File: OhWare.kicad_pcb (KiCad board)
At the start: 2 copper layers, 110 parts, among them J1 Screw_Terminal_01x03, J11 Screw_Terminal_01x05, J12 Conn_01x03_Pin, J13 Micro_SD_Card, J14 Screw_Terminal_01x03, J15 RJ45_Hanrun_HR911105A_Horizon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, J16 Conn_02x05_Odd_Even, J17 Conn_02x03_Odd_Even, J18 Conn_02x03_Odd_Even, J19 Conn_02x03_Odd_Even, J2 Conn_01x04_Pin, J3 Conn_01x02_Pin, J4 Conn_01x02_Pin, J5 Conn_01x04_Pin, J6 Conn_01x02_Pin, J7 8P8C_Shielded, J8 8P8C_Shielded, J9 Conn_02x05_Odd_Even, SW2 SW_DIP_x01, SW3 SW_DIP_x03, U1 STM32F407VETx, U2 SIT65HVD230DR, U3 SIT3490EESA, U4 XL1509-5.0E1, U5 AMS1117-3.3, U6 TL431M-0.3%-6AF, U7 LAN8720AI-CP-TR, U8 USB-TYPE-C-016, X1 X32258MOB4SI, X2 ABS07-32.768KHZ-T, X3 XL2EL89CSI-111YLC-25M

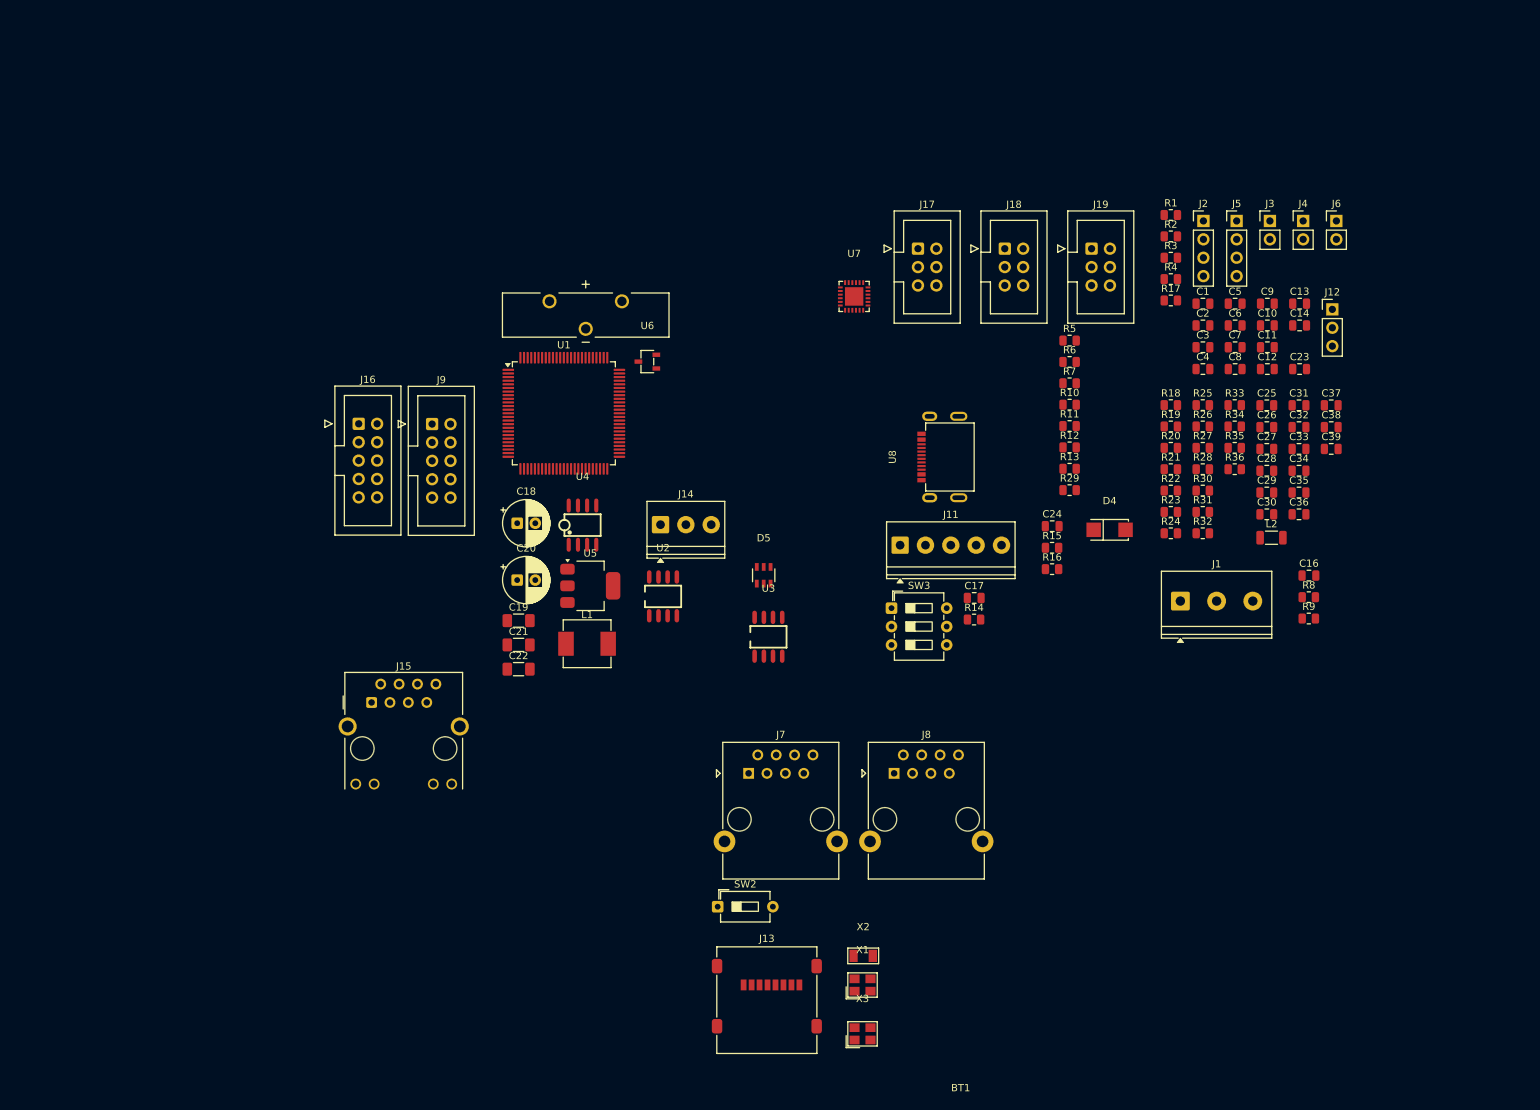
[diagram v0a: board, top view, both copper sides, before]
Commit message: Key CHanges for connector choices , termination and semi-final decisions on them
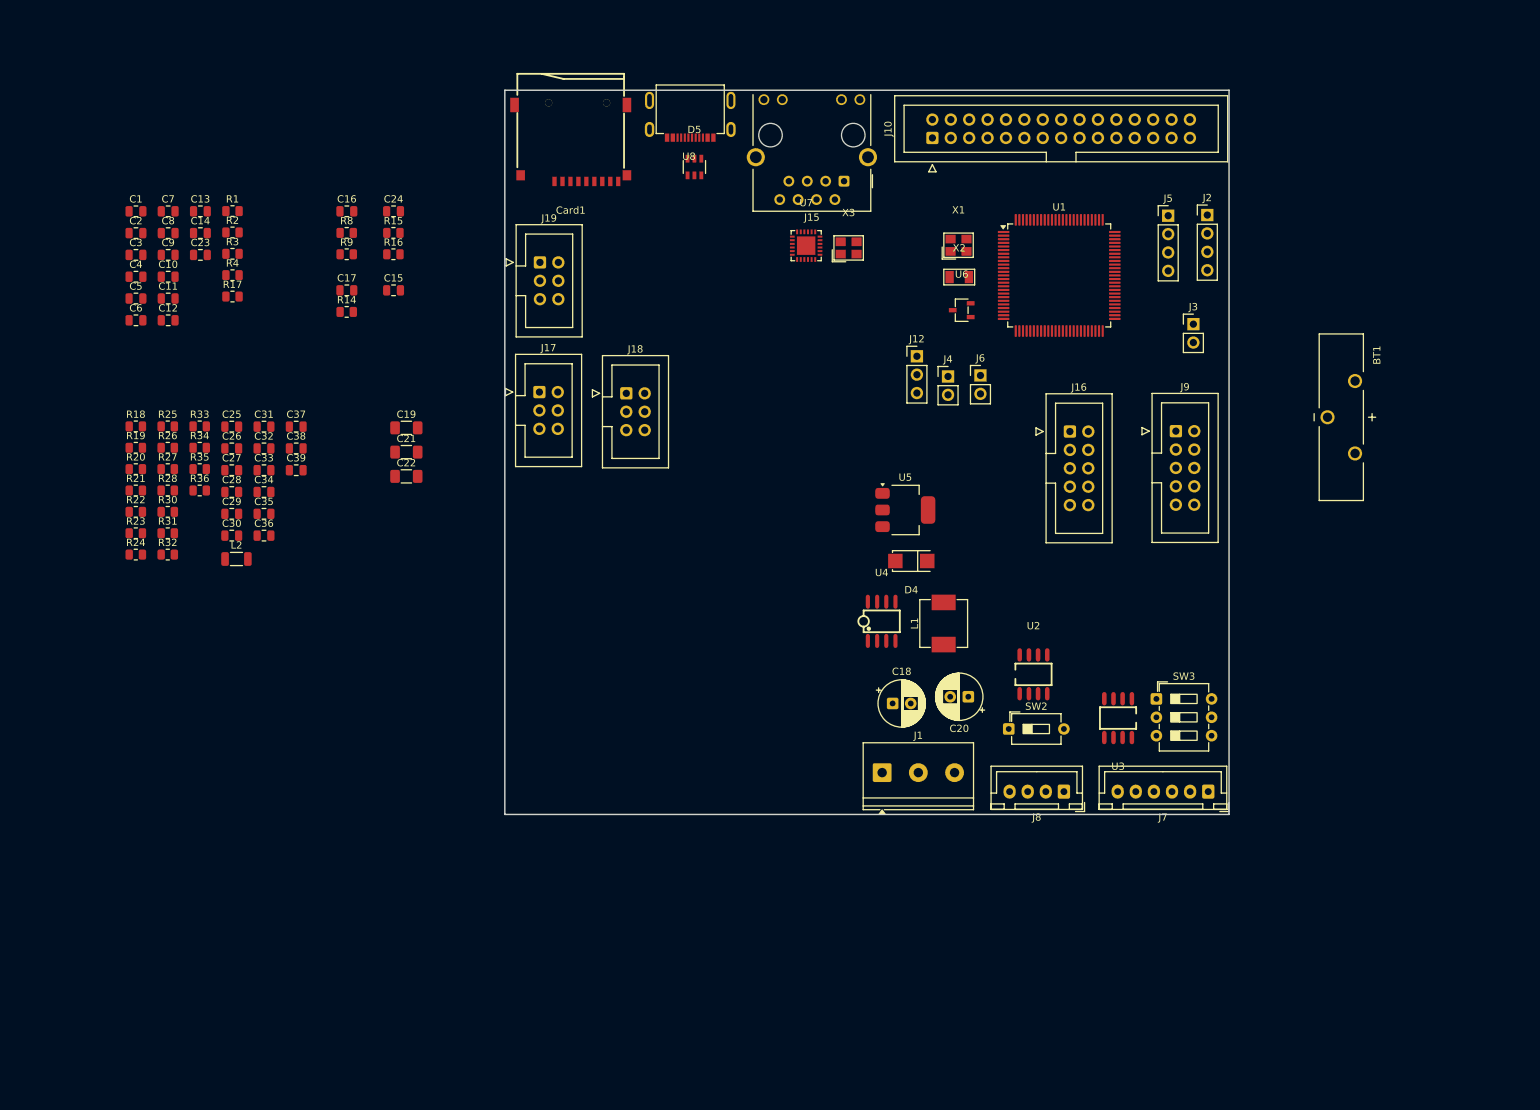
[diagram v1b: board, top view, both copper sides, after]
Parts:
- removed J11: Screw_Terminal_01x05, TerminalBlock_Phoenix:TerminalBlock_Phoenix_PT-1,5-5-3.5-H_1x05_P3.50mm_Horizontal
- removed J13: Micro_SD_Card, Connector_Card:microSD_HC_Molex_47219-2001
- removed J14: Screw_Terminal_01x03, TerminalBlock_Phoenix:TerminalBlock_Phoenix_PT-1,5-3-3.5-H_1x03_P3.50mm_Horizontal
- removed R10, R11, R12, R13, R29, R5, R6, R7: 0, Resistor_SMD:R_0805_2012Metric
- added C15: 100n, Capacitor_SMD:C_0805_2012Metric, F.Cu at (84.6, 77.6)
- added Card1: TF-01A, EasyEDA:TF-SMD_TF-01A, F.Cu at (109.1, 57.3)
- added J10: Conn_02x15_Odd_Even, Connector_IDC:IDC-Header_2x15_P2.54mm_Vertical, F.Cu at (159.0, 56.6)
- J7: value 8P8C_Shielded -> Conn_01x06_Pin; footprint Connector_RJ:RJ45_Ninigi_GE -> Connector_JST:JST_XH_B6B-XH-A_1x06_P2.50mm_Vertical
- J8: value 8P8C_Shielded -> Conn_01x04_Pin; footprint Connector_RJ:RJ45_Ninigi_GE -> Connector_JST:JST_XH_B4B-XH-A_1x04_P2.50mm_Vertical
- moved C23 152.6 mm to (58.0, 72.7)
- moved C13 152.3 mm to (58.0, 66.7)
- moved C14 152.3 mm to (58.0, 69.7)
- moved C10 151.9 mm to (53.5, 75.8)
- moved C11 151.9 mm to (53.5, 78.8)
- moved C12 151.9 mm to (53.5, 81.8)
- moved C9 151.9 mm to (53.5, 72.7)
- moved C5 151.8 mm to (49.1, 78.8)
- moved C6 151.8 mm to (49.1, 81.8)
- moved C7 148.5 mm to (53.5, 66.7)
- moved C8 148.5 mm to (53.5, 69.7)
- moved C1 147.9 mm to (49.1, 66.7)
- moved C2 147.9 mm to (49.1, 69.7)
- moved C3 147.9 mm to (49.1, 72.7)
- moved C4 147.9 mm to (49.1, 75.8)
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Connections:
- J15 pad SH: Earth -> GND
- J16 pad 3: Net-(J16-Pin_3) -> /Controller/SPI1_MOSI
- J16 pad 5: Net-(J16-Pin_5) -> /Controller/SPI1_MISO
- J16 pad 7: Net-(J16-Pin_7) -> /Controller/SPI1_SCK
- J16 pad 9: Net-(J16-Pin_9) -> /Controller/SPI1_CS2
- J7 pad 1: /CAN/CAN_H -> /RS485/Y
- J7 pad 2: /CAN/CAN_L -> /RS485/Z
- J7 pad 3: GND -> /RS485/A
- J7 pad 4: unconnected-(J7-Pad4) -> /RS485/B
- J7 pad 5: unconnected-(J7-Pad5) -> GND
- J7 pad 6: unconnected-(J7-Pad6) -> Earth
- J8 pad 4: unconnected-(J8-Pad4) -> Earth
- J9 pad 3: Net-(J9-Pin_3) -> /Controller/SPI1_MOSI
- J9 pad 5: Net-(J9-Pin_5) -> /Controller/SPI1_MISO
- J9 pad 7: Net-(J9-Pin_7) -> /Controller/SPI1_SCK
- J9 pad 9: Net-(J9-Pin_9) -> /Controller/SPI1_CS1
- U8 pad 17: Earth -> GND
- U8 pad 18: Earth -> GND
- U8 pad A1: unconnected-(U8-PadA1) -> GND
- U8 pad A12: unconnected-(U8-PadA12) -> Net-(U8-PadA12)
- U8 pad B1: unconnected-(U8-PadB1) -> Net-(U8-PadA12)
- U8 pad B12: unconnected-(U8-PadB12) -> GND
- U8 pad B6: unconnected-(U8-PadB6) -> Net-(D5-Pad3)
- U8 pad B7: unconnected-(U8-PadB7) -> Net-(D5-Pad1)
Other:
- board outline added: 100 x 100 mm

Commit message: Done routing for Buck Converter , Rs485 and CAN , Some Routing for MCU and associated circuitry , NO ETHERNET ROUTING , NO module Interconnects yet
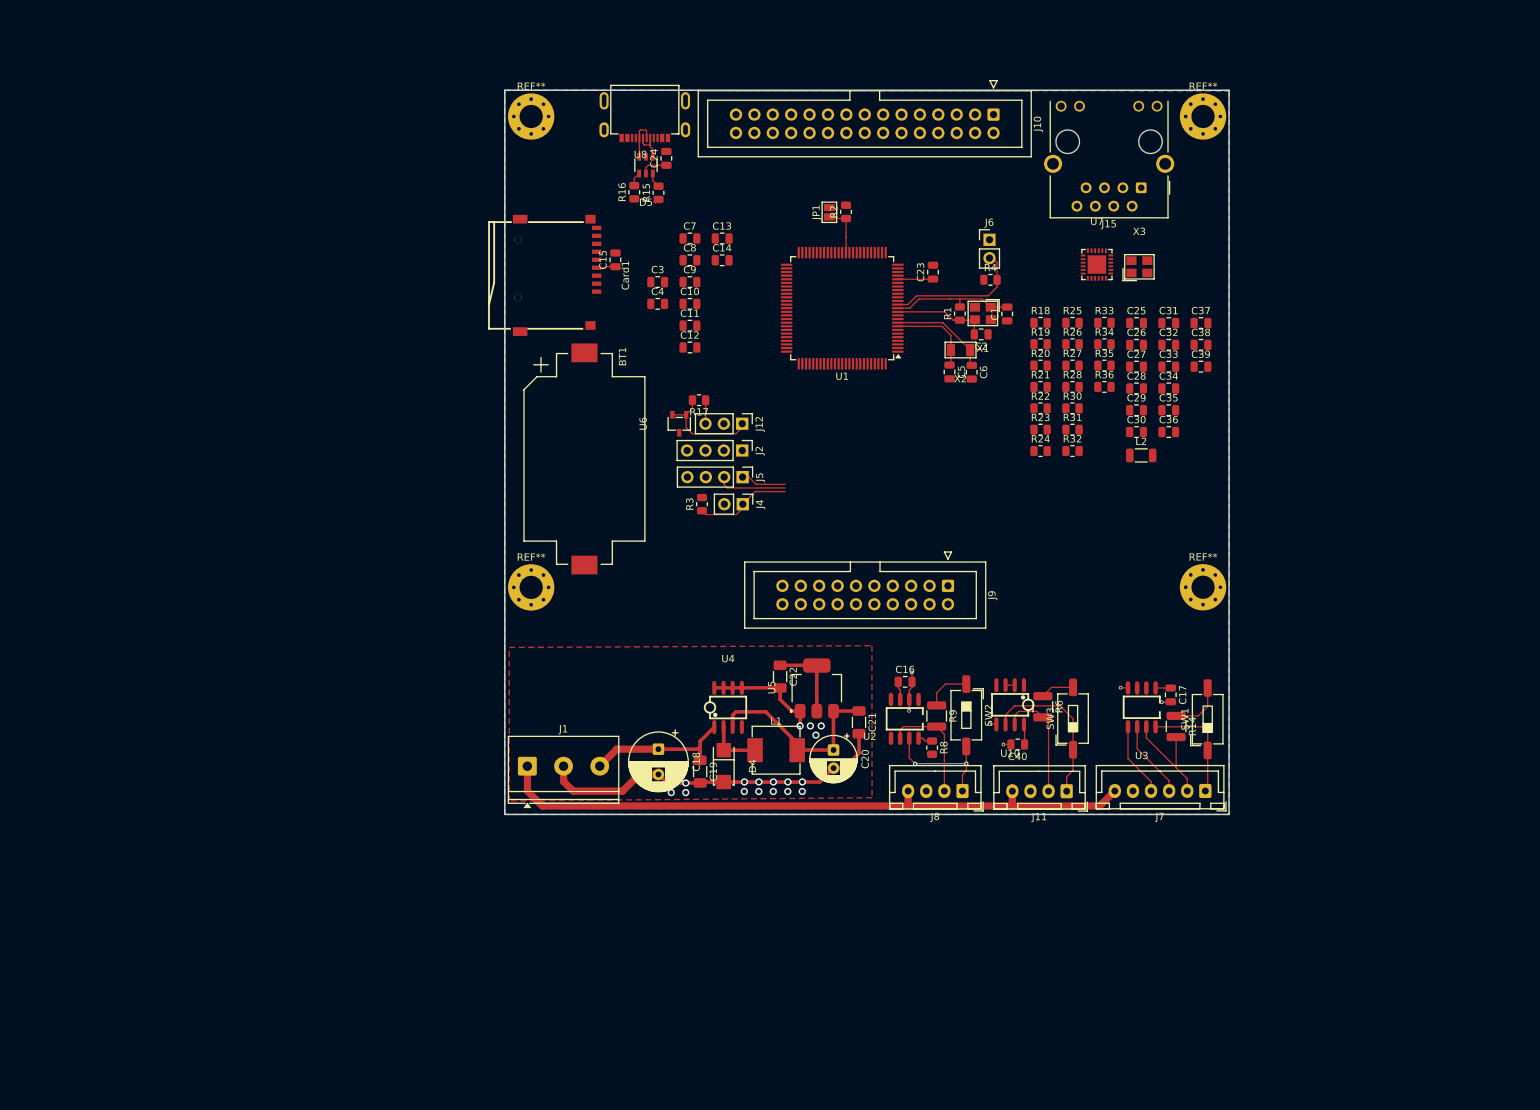
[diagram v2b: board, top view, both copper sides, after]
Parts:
- removed J16: Conn_02x05_Odd_Even, Connector_IDC:IDC-Header_2x05_P2.54mm_Vertical
- removed J17, J18, J19: Conn_02x03_Odd_Even, Connector_IDC:IDC-Header_2x03_P2.54mm_Vertical
- removed J3: Conn_01x02_Pin, Connector_PinHeader_2.54mm:PinHeader_1x02_P2.54mm_Vertical
- added C40: 0.1u, Capacitor_SMD:C_0805_2012Metric, F.Cu at (170.8, 140.3)
- added J11: Conn_01x04_Pin, Connector_JST:JST_XH_B4B-XH-A_1x04_P2.50mm_Vertical, F.Cu at (177.6, 146.8)
- added JP1: Jumper_2_Open, Jumper:SolderJumper-2_P1.3mm_Open_Pad1.0x1.5mm, F.Cu at (144.8, 66.9)
- added R6: 120, Resistor_SMD:R_1210_3225Metric, F.Cu at (174.3, 135.1)
- added REF**: MountingHole_3.2mm_M3_Pad_Via, MountingHole:MountingHole_3.2mm_M3_Pad_Via, F.Cu at (103.6, 53.6)
- added REF**: MountingHole_3.2mm_M3_Pad_Via, MountingHole:MountingHole_3.2mm_M3_Pad_Via, F.Cu at (103.6, 118.7)
- added REF**: MountingHole_3.2mm_M3_Pad_Via, MountingHole:MountingHole_3.2mm_M3_Pad_Via, F.Cu at (196.4, 53.6)
- added REF**: MountingHole_3.2mm_M3_Pad_Via, MountingHole:MountingHole_3.2mm_M3_Pad_Via, F.Cu at (196.4, 118.6)
- added SW1: SW_DIP_x01, Button_Switch_SMD:SW_DIP_SPSTx01_Slide_6.7x4.1mm_W8.61mm_P2.54mm_LowProfile, F.Cu at (197.1, 136.8)
- added U10: SP3485EN-L/TR, EasyEDA:SOIC-8_L5.0-W4.0-P1.27-LS6.0-BL, F.Cu at (169.8, 134.9)
- BT1: footprint EasyEDA:BAT_1074 -> Battery:BatteryHolder_Keystone_1060_1x2032
- C18: footprint Capacitor_THT:CP_Radial_D6.3mm_P2.50mm -> Capacitor_THT:CP_Radial_D8.0mm_P3.50mm
- J15: footprint Connector_RJ:RJ45_Hanrun_HR911105A_Horizontal -> EasyEDA:RJ45_Hanrun_HR911105A_Horizontal
- J9: value Conn_02x05_Odd_Even -> Conn_02x10_Odd_Even; footprint Connector_IDC:IDC-Header_2x05_P2.54mm_Vertical -> Connector_IDC:IDC-Header_2x10_P2.54mm_Vertical
- R14, R9: footprint Resistor_SMD:R_0805_2012Metric -> Resistor_SMD:R_1210_3225Metric
- SW2: footprint Button_Switch_THT:SW_DIP_SPSTx01_Slide_6.7x4.1mm_W7.62mm_P2.54mm_LowProfile -> Button_Switch_SMD:SW_DIP_SPSTx01_Slide_6.7x4.1mm_W8.61mm_P2.54mm_LowProfile
- SW3: value SW_DIP_x03 -> SW_DIP_x01; footprint Button_Switch_THT:SW_DIP_SPSTx03_Slide_6.7x9.18mm_W7.62mm_P2.54mm_LowProfile -> Button_Switch_SMD:SW_DIP_SPSTx01_Slide_6.7x4.1mm_W8.61mm_P2.54mm_LowProfile
- moved R14 128.0 mm to (192.7, 137.8), turned to -90 degrees
- moved C17 126.7 mm to (191.9, 133.5), turned to -90 degrees
- moved C31 125.7 mm to (191.7, 82.2)
- moved C32 125.7 mm to (191.7, 85.2)
- moved C33 125.7 mm to (191.7, 88.2)
- moved C34 125.7 mm to (191.7, 91.2)
- moved C35 125.7 mm to (191.7, 94.2)
- moved C36 125.7 mm to (191.7, 97.2)
- moved C37 125.7 mm to (196.1, 82.2)
- moved C38 125.7 mm to (196.1, 85.2)
- moved C39 125.7 mm to (196.1, 88.2)
- moved L2 125.7 mm to (187.9, 100.4)
- moved C25 125.7 mm to (187.2, 82.2)
- moved C26 125.7 mm to (187.2, 85.2)
- moved C27 125.7 mm to (187.2, 88.2)
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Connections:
- J1 pad 1: +12V -> Earth
- J1 pad 3: Earth -> +12V
- J7 pad 1: /RS485/Y -> /RS485/A
- J7 pad 2: /RS485/Z -> /RS485/B
- J7 pad 3: /RS485/A -> /RS485/Z
- J7 pad 4: /RS485/B -> /RS485/Y
- J9 pad 1: +5V -> /Controller/SPI1_MOSI
- J9 pad 10: GND -> /Controller/UART3_Rx
- J9 pad 2: GND -> /Controller/SPI1_MISO
- J9 pad 3: /Controller/SPI1_MOSI -> /Controller/SPI1_SCK
- J9 pad 4: GND -> /Controller/SPI1_CS1
- J9 pad 5: /Controller/SPI1_MISO -> /Controller/SPI1_CS2
- J9 pad 6: GND -> /SPI_I2C_UART_expansion/SPI1_CS3
- J9 pad 7: /Controller/SPI1_SCK -> /SPI_I2C_UART_expansion/SPI1_CS4
- J9 pad 9: /Controller/SPI1_CS1 -> /Controller/UART3_Tx
- SW3 pad 1: /RS485/A -> /RS485/A2
- SW3 pad 2: /RS485/A -> Net-(R6-Pad1)
- U1 pad 7: unconnected-(U1-PC13-Pad7) -> /Controller/ETH_nRST
- U1 pad 88: /Controller/ETH_nRST -> /Controller/RS485_nRE/DE
- U8 pad A12: Net-(U8-PadA12) -> GND
- U8 pad B1: Net-(U8-PadA12) -> GND
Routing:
- net Earth: track 0.00 -> 89.5 mm
- net GND: track 0.00 -> 75.7 mm, vias 0 -> 24
- net +5V: track 0.00 -> 27.4 mm
- net +3.3V: track 0.00 -> 22.5 mm
- net /RS485/A2: track 0.00 -> 22.3 mm
- net +12V: track 0.00 -> 20.4 mm
- net /Controller/NRST: track 0.00 -> 19.4 mm
- net Net-(U1-PH1): track 0.00 -> 17.3 mm
- net /CAN/CAN_H: track 0.00 -> 17.3 mm, vias 0 -> 2
- net /RS485/B2: track 0.00 -> 16.2 mm
- net /CAN/CAN_L: track 0.00 -> 15.8 mm
- net /RS485/A: track 0.00 -> 15.7 mm
- net /RS485/B: track 0.00 -> 15.4 mm
- net /Controller/VREF_2.5V: track 0.00 -> 15.0 mm
- net Net-(U1-PH0): track 0.00 -> 14.0 mm
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- added copper zone on B.Cu, net GND
- added copper zone on F.Cu, net GND
